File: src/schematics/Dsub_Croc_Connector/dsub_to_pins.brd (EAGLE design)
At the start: 71 x 36.5 mm, 39 parts

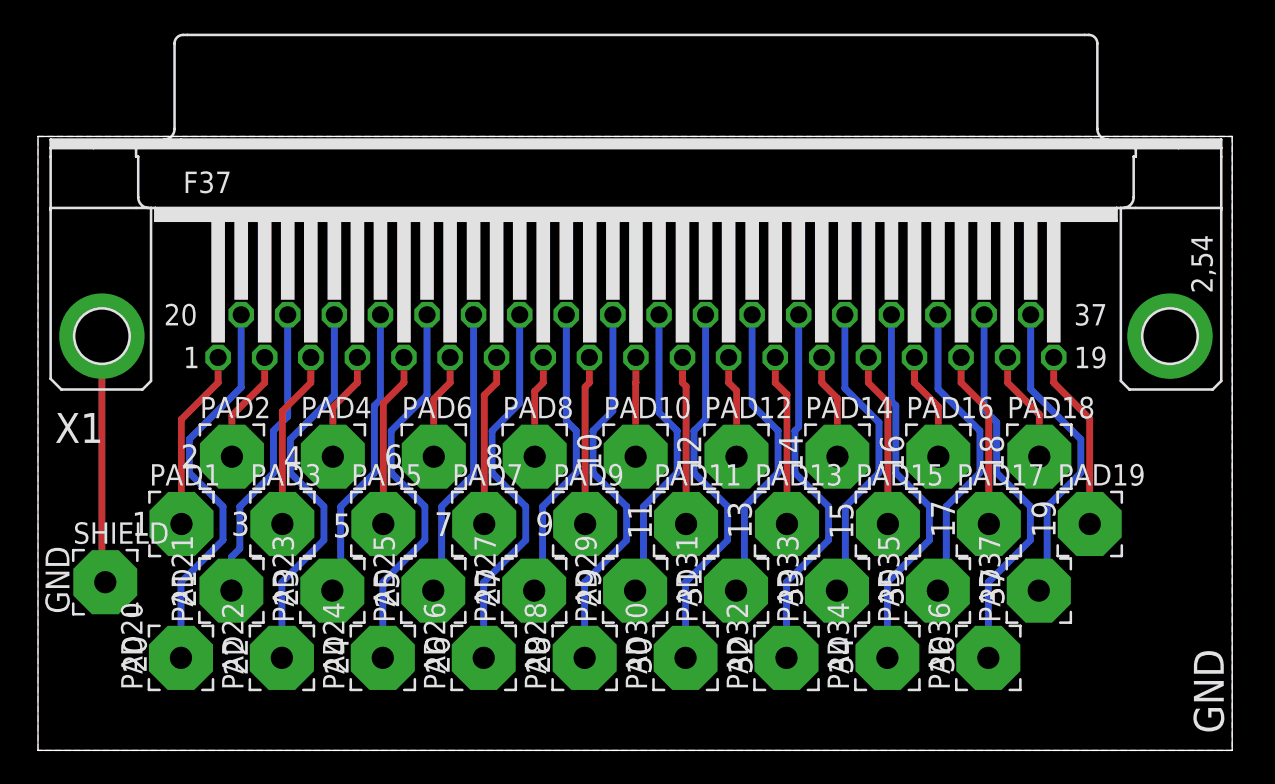
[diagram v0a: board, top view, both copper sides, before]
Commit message: New Debug phantom, and new Dsub adaptors. With Gerbers sent to PCBWay
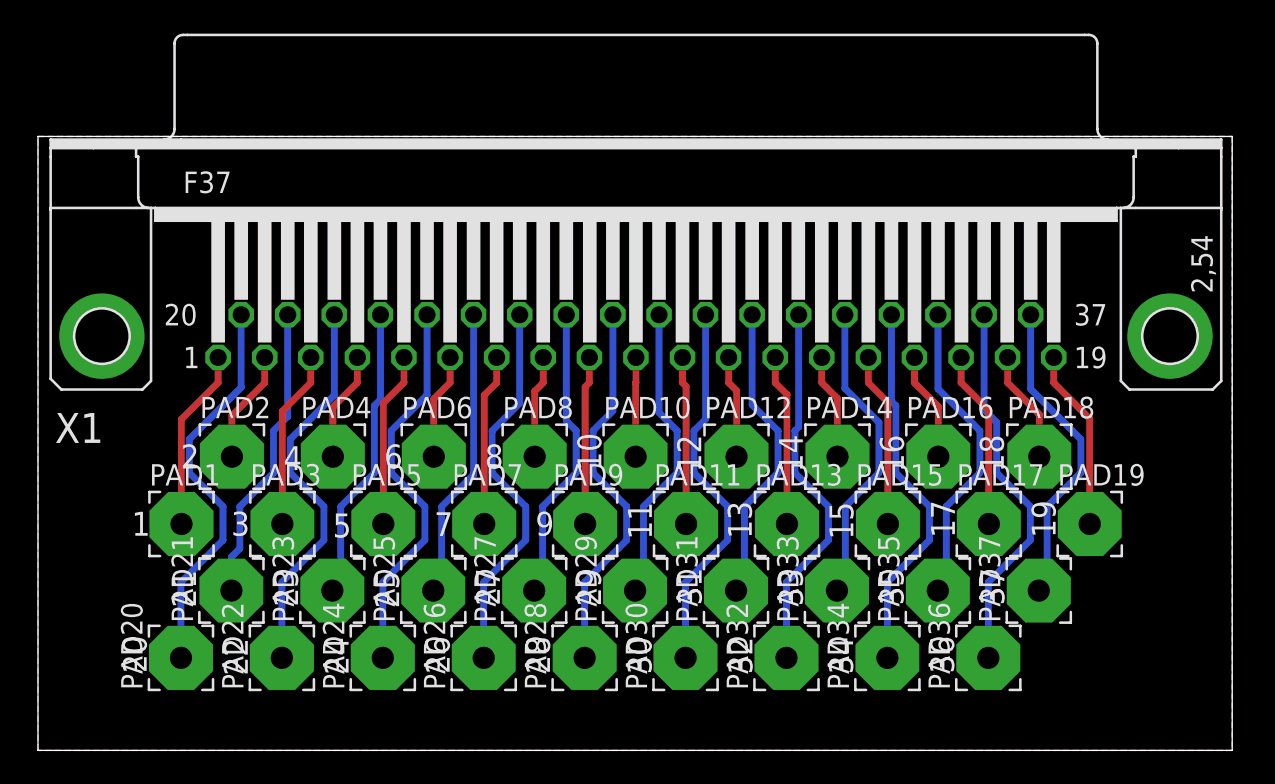
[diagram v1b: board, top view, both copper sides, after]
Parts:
- removed SHIELD: WIREPAD3,81/1,3, wirepad:3,81/1,3
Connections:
- removed net GND: SHIELD.1, X1.G1, X1.G2
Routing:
- net GND: track 14.7 -> 0.00 mm
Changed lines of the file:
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@@
 <grid distance="0.5" unitdist="mm" unit="mm" style="dots" multiple="1" display="yes" altdistance="0.05" altunitdist="mm" altunit="mm"/>
 <layers>
-<layer number="1" name="Top" color="4" fill="1" visible="no" active="yes"/>
+<layer number="1" name="Top" color="4" fill="1" visible="yes" active="yes"/>
 <layer number="2" name="Route2" color="1" fill="3" visible="no" active="no"/>
 <layer number="3" name="Route3" color="4" fill="3" visible="no" active="no"/>
@@
 <layer number="14" name="Route14" color="1" fill="6" visible="no" active="no"/>
 <layer number="15" name="Route15" color="4" fill="6" visible="no" active="no"/>
-<layer number="16" name="Bottom" color="1" fill="1" visible="no" active="yes"/>
+<layer number="16" name="Bottom" color="1" fill="1" visible="yes" active="yes"/>
 <layer number="17" name="Pads" color="2" fill="1" visible="yes" active="yes"/>
 <layer number="18" name="Vias" color="2" fill="1" visible="yes" active="yes"/>
@@
 <text x="94.745" y="68.638" size="1.4224" layer="112" font="vector" ratio="12" rot="R270" align="center">34</text>
 <text x="97.751" y="72.738" size="1.4224" layer="112" font="vector" ratio="12" rot="R270" align="center">35</text>
-<text x="48.16" y="73.135" size="1.4224" layer="112" font="vector" ratio="12" rot="R90" align="center">GND</text>
-<polygon width="0.4064" layer="29">
-<vertex x="108.96" y="63.19"/>
-<vertex x="108.96" y="68.175" curve="-90"/>
-<vertex x="110.96" y="70.175"/>
-<vertex x="112.675" y="70.175" curve="-90"/>
-<vertex x="114.675" y="68.175"/>
-<vertex x="114.675" y="63.19"/>
-</polygon>
-<polygon width="0.4064" layer="30">
-<vertex x="114.675" y="63.19"/>
-<vertex x="114.675" y="68.175" curve="90"/>
-<vertex x="112.675" y="70.175"/>
-<vertex x="110.96" y="70.175" curve="90"/>
-<vertex x="108.96" y="68.175"/>
-<vertex x="108.96" y="63.19"/>
-</polygon>
-<polygon width="0.4064" layer="30">
-<vertex x="114.54" y="63.19"/>
-<vertex x="114.54" y="68.175" curve="90"/>
-<vertex x="112.54" y="70.175"/>
-<vertex x="110.825" y="70.175" curve="90"/>
-<vertex x="108.825" y="68.175"/>
-<vertex x="108.825" y="63.19"/>
-</polygon>
-<polygon width="0.4064" layer="29">
-<vertex x="108.825" y="63.19"/>
-<vertex x="108.825" y="68.175" curve="-90"/>
-<vertex x="110.825" y="70.175"/>
-<vertex x="112.54" y="70.175" curve="-90"/>
-<vertex x="114.54" y="68.175"/>
-<vertex x="114.54" y="63.19"/>
-</polygon>
 <text x="57.927" y="76.473" size="1.4224" layer="22" font="vector" ratio="12" rot="MR0" align="center">1</text>
 <text x="60.933" y="80.473" size="1.4224" layer="22" font="vector" ratio="12" rot="MR0" align="center">2</text>
@@
 <text x="53.76" y="73.135" size="1.4224" layer="22" font="vector" ratio="12" rot="MR90" align="center">GND</text>
 <text x="63.5" y="64" size="1.778" layer="22" font="vector" rot="MR0">Jimmy 2016</text>
-<text x="115.5" y="64" size="1.778" layer="22" font="vector" rot="MR90">GND</text>
-<text x="117.5" y="64" size="1.778" layer="112" font="vector" rot="R90">GND</text>
 <text x="66.5" y="98.5" size="2.54" layer="22" font="vector" ratio="17" rot="MR180">DSUB TO WIRES</text>
 <text x="108" y="64" size="1.27" layer="22" font="vector" rot="MR0">github.com/EIT-team/ScouseTom</text>
@@
 <element name="PAD36" library="wirepad" package="3,81/1,3" value="WIREPAD3,81/1,3" x="103.5" y="68.5" rot="R90"/>
 <element name="PAD37" library="wirepad" package="3,81/1,3" value="WIREPAD3,81/1,3" x="106.5" y="72.5" rot="R90"/>
-<element name="SHIELD" library="wirepad" package="3,81/1,3" value="WIREPAD3,81/1,3" x="51" y="73"/>
 </elements>
 <signals>
 <signal name="GND">
-<contactref element="X1" pad="G1"/>
-<contactref element="SHIELD" pad="1"/>
-<wire x1="50.8" y1="87.63" x2="50.8" y2="73.2" width="0.4064" layer="1"/>
-<wire x1="50.8" y1="73.2" x2="51" y2="73" width="0.4064" layer="1"/>
 <polygon width="0.4064" layer="1">
 <vertex x="47" y="99.5"/>
@@
 <vertex x="47" y="63"/>
 </polygon>
-<contactref element="X1" pad="G2"/>
 <polygon width="0.4064" layer="16">
 <vertex x="47" y="99.5"/>
